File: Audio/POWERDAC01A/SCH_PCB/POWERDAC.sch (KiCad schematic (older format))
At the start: 2 parts

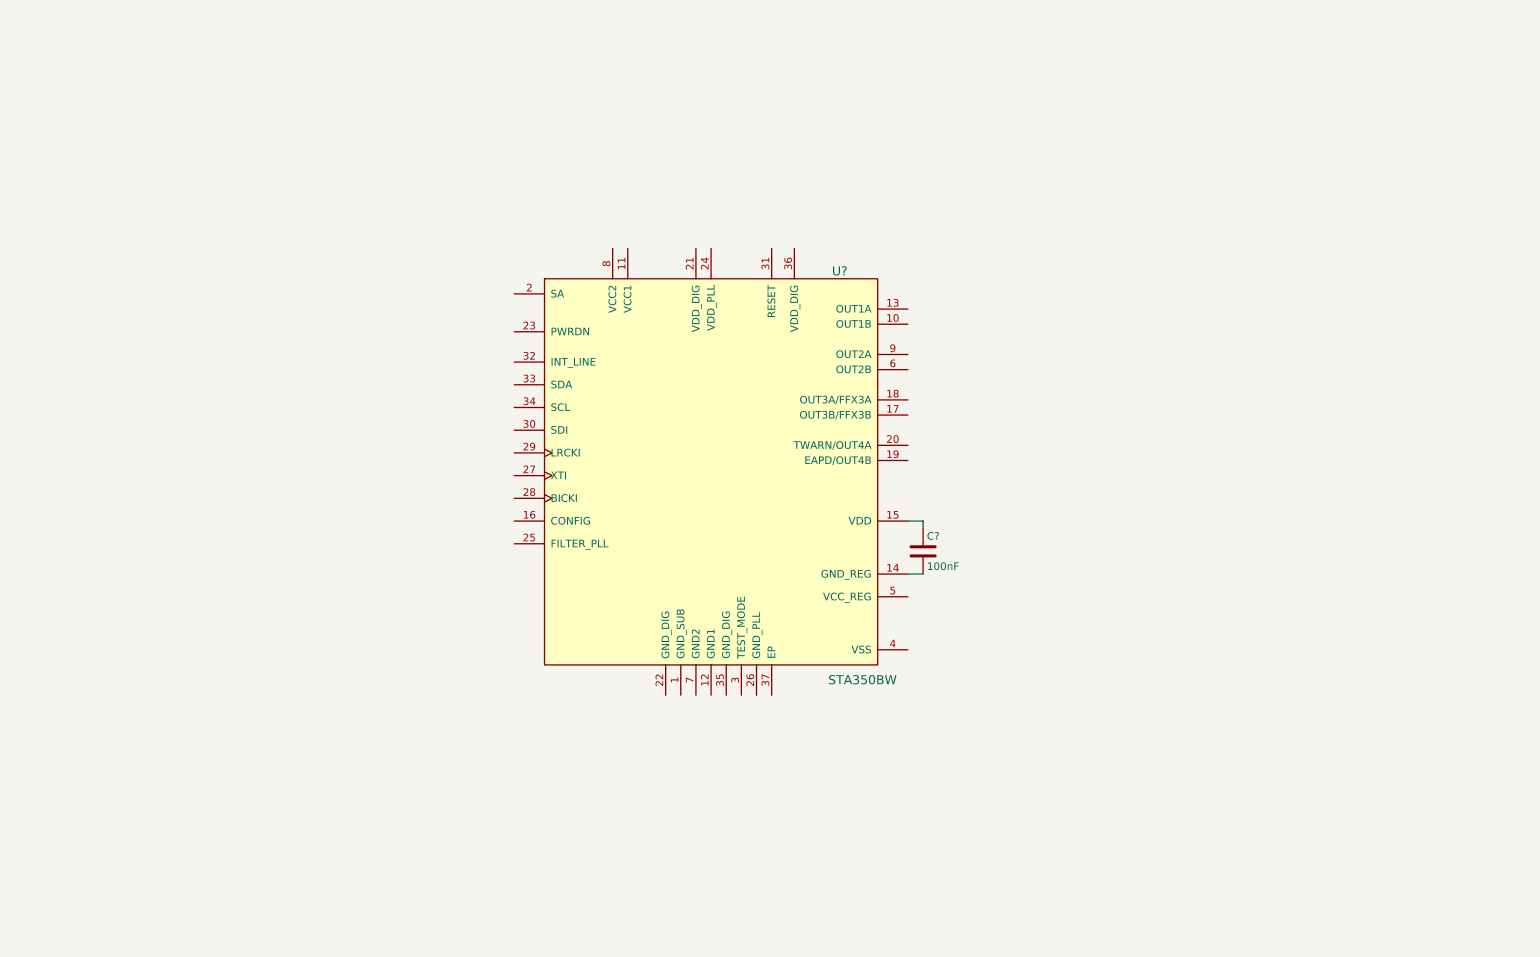
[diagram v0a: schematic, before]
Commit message: uprava prumeru hridele podle nastaveni tiskarny.
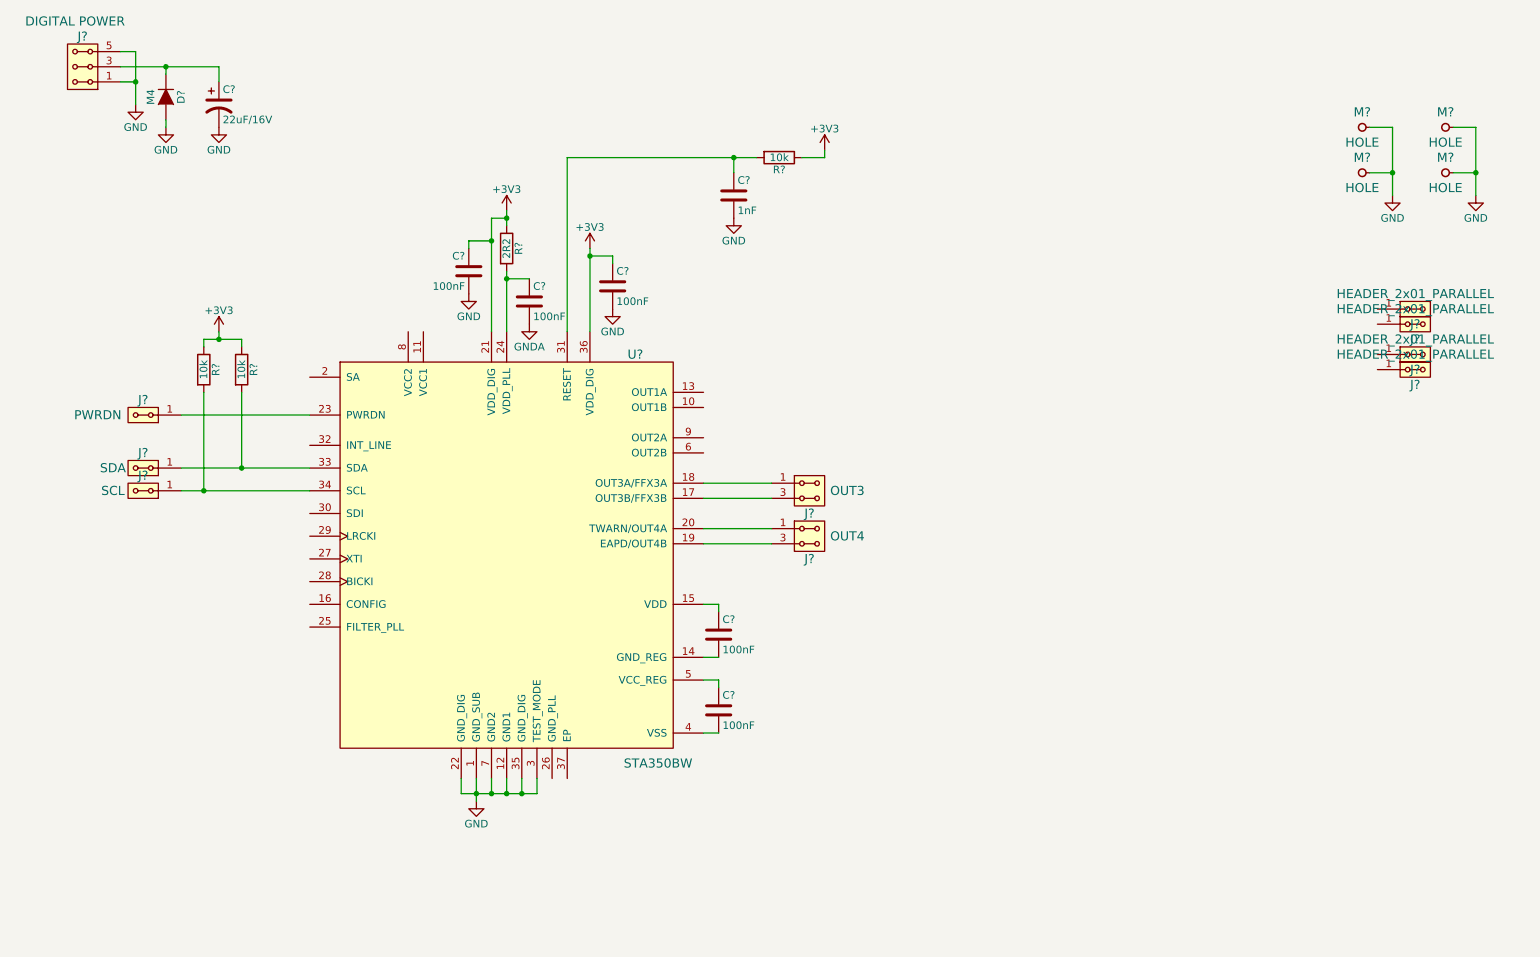
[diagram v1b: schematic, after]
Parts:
- added C? (x4): 100nF, symbol C
- added C?: 1nF, symbol C
- added C?: 22uF/16V, symbol CP1
- added D?: M4, symbol D
- added J?: PWRDN, symbol HEADER_2x01_PARALLEL
- added J?: OUT3, symbol HEADER_2x02_PARALLEL
- added J?: OUT4, symbol HEADER_2x02_PARALLEL
- added J? (x4): HEADER_2x01_PARALLEL, symbol HEADER_2x01_PARALLEL
- added J?: SDA, symbol HEADER_2x01_PARALLEL
- added J?: SCL, symbol HEADER_2x01_PARALLEL
- added J?: DIGITAL POWER, symbol HEADER_2x03_PARALLEL
- added M? (x4): HOLE, symbol HOLE
- added R? (x3): 10k, symbol R
- added R?: 2R2, symbol R
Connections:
- net GND: now reaches U?.1 (GND_SUB)
- net GND: now also U?.12 (GND1), U?.22 (GND_DIG), U?.3 (TEST_MODE), U?.35 (GND_DIG), U?.7 (GND2), C?.2, C?.2, C?.2, C?.2, D?.2 (A), J?.1, J?.2, J?.5, J?.6, M?.1, M?.1, M?.1, M?.1
- net at U?.17 (OUT3B/FFX3B): now also J?.3, J?.4
- net at U?.18 (OUT3A/FFX3A): now also J?.1, J?.2
- net at U?.19 (EAPD/OUT4B): now also J?.3, J?.4
- net at U?.20 (TWARN/OUT4A): now also J?.1, J?.2
- net +3V3: now reaches U?.21 (VDD_DIG)
- net +3V3: now also U?.36 (VDD_DIG), C?.1, C?.1, R?.1, R?.1, R?.1, R?.1
- net at U?.23 (PWRDN): now also J?.1, J?.2
- net at U?.24 (VDD_PLL): now also C?.1, R?.2
- net at U?.31 (RESET): now also C?.1, R?.2
- net at U?.33 (SDA): now also J?.1, J?.2, R?.2
- net at U?.34 (SCL): now also J?.1, J?.2, R?.2
- net at U?.4 (VSS): now also C?.2
- net at U?.5 (VCC_REG): now also C?.1
- new net: J?.1, J?.2 (x4)
- new net: C?.1, D?.1 (K), J?.3, J?.4
- new net GNDA: C?.2
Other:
- moved on the sheet: C?, U?

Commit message: zacatek navrhu noveho PCB pro modul vykonoveho zesilovace.
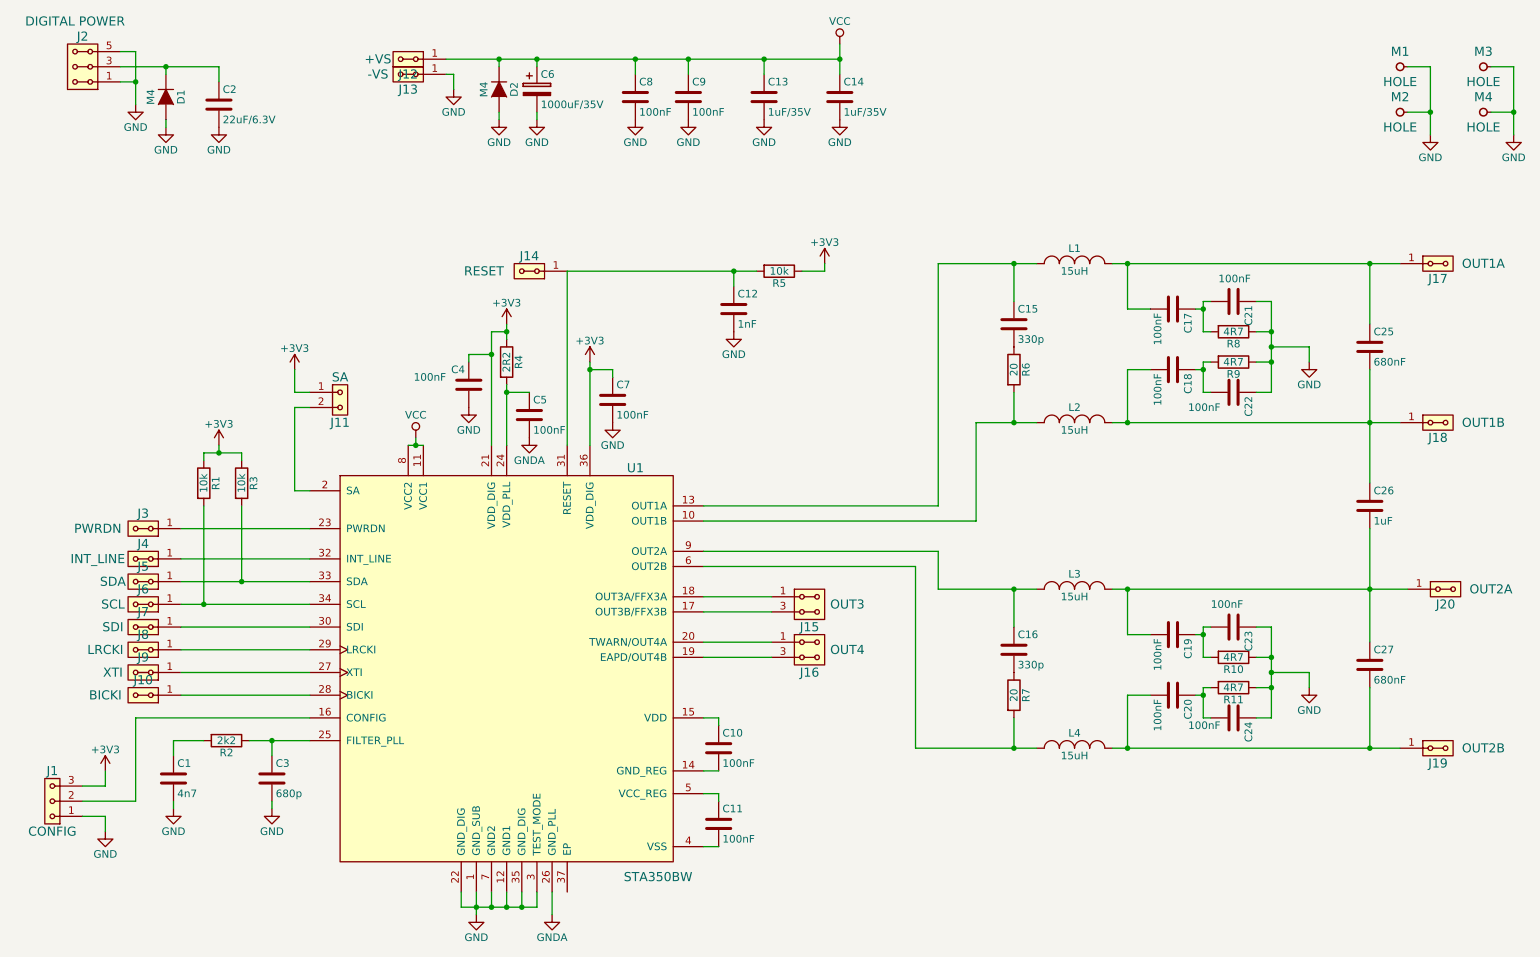
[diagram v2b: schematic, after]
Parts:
- removed C?: 22uF/16V, symbol CP1
- removed J? (x2): HEADER_2x01_PARALLEL, symbol HEADER_2x01_PARALLEL
- added C1: 4n7, Capacitors_SMD:C_0805, symbol C
- added C13, C14: 1uF/35V, Capacitors_SMD:C_1206, symbol C
- added C15, C16: 330p, Capacitors_SMD:C_0805, symbol C
- added C17, C18, C19, C20, C21, C22, C23, C24, C8, C9: 100nF, Capacitors_SMD:C_0805, symbol C
- added C2: 22uF/6.3V, Capacitors_SMD:C_0805, symbol C
- added C25, C27: 680nF, Capacitors_SMD:C_0805, symbol C
- added C26: 1uF, Capacitors_SMD:C_0805, symbol C
- added C3: 680p, Capacitors_SMD:C_0805, symbol C
- added C6: 1000uF/35V, Capacitors_ThroughHole:C_Radial_D12.5_L25_P5, symbol CP
- added D2: M4, Diodes_SMD:SMA_Standard, symbol D
- added J1: CONFIG, Mlab_Pin_Headers:Straight_1x03, symbol HEADER_1x03
- added J10: BICKI, Mlab_Pin_Headers:Straight_1x02, symbol HEADER_2x01_PARALLEL
- added J11: SA, Mlab_Pin_Headers:Straight_1x02, symbol HEADER_1x02
- added J12: +VS, Terminal_Blocks:TerminalBlock_WAGO_256_RM5mm_1pol, symbol HEADER_2x01_PARALLEL
- added J13: -VS, Terminal_Blocks:TerminalBlock_WAGO_256_RM5mm_1pol, symbol HEADER_2x01_PARALLEL
- added J14: RESET, Mlab_Pin_Headers:Straight_1x02, symbol HEADER_2x01_PARALLEL
- added J19: OUT2B, Terminal_Blocks:TerminalBlock_WAGO_256_RM5mm_1pol, symbol HEADER_2x01_PARALLEL
- added J20: OUT2A, Terminal_Blocks:TerminalBlock_WAGO_256_RM5mm_1pol, symbol HEADER_2x01_PARALLEL
- added J4: INT_LINE, Mlab_Pin_Headers:Straight_1x02, symbol HEADER_2x01_PARALLEL
- added J7: SDI, Mlab_Pin_Headers:Straight_1x02, symbol HEADER_2x01_PARALLEL
- added J8: LRCKI, Mlab_Pin_Headers:Straight_1x02, symbol HEADER_2x01_PARALLEL
- added J9: XTI, Mlab_Pin_Headers:Straight_1x02, symbol HEADER_2x01_PARALLEL
- added L1, L2, L3, L4: 15uH, Choke_SMD:Choke_SMD_12x12mm_h6mm, symbol INDUCTOR_SMALL
- added R10, R11, R8, R9: 4R7, Resistors_SMD:R_1206, symbol R
- added R2: 2k2, Resistors_SMD:R_0805, symbol R
- added R6, R7: 20, Resistors_SMD:R_1206, symbol R
- C10, C11, C12, C4, C5, C7: renamed from C?; footprint (none) -> Capacitors_SMD:C_0805
- D1: renamed from D?; footprint (none) -> Diodes_SMD:SMA_Standard
- J15, J16: renamed from J?; footprint (none) -> Mlab_Pin_Headers:Straight_2x02
- J17: renamed from J?; value HEADER_2x01_PARALLEL -> OUT1A; footprint (none) -> Terminal_Blocks:TerminalBlock_WAGO_256_RM5mm_1pol
- J18: renamed from J?; value HEADER_2x01_PARALLEL -> OUT1B; footprint (none) -> Terminal_Blocks:TerminalBlock_WAGO_256_RM5mm_1pol
- J2: renamed from J?; footprint (none) -> Mlab_Pin_Headers:Straight_2x03
- J3, J5, J6: renamed from J?; footprint (none) -> Mlab_Pin_Headers:Straight_1x02
- M1, M2, M3, M4: renamed from M?; footprint (none) -> Mlab_Mechanical:MountingHole_3mm
- R1, R3, R4, R5: renamed from R?; footprint (none) -> Resistors_SMD:R_0805
- U1: renamed from U?; footprint (none) -> Power_Packages_SMD:PowerSSO-36
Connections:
- net +3V3: now also J1.3, J11.1
- net GND: now also C1.2, C13.2, C14.2, C2.2, C21.1, C22.1, C23.1, C24.1, C3.2, C6.2, C8.2, C9.2, D2.2 (A), J1.1, J13.1, J13.2, R10.1, R11.1, R8.1, R9.1
- net GNDA: now also U1.26 (GND_PLL)
- net at U1.10 (OUT1B): now also L2.1, R6.2
- net VCC: now reaches U1.11 (VCC1)
- net VCC: now also U1.8 (VCC2), C13.1, C14.1, C6.1, C8.1, C9.1, D2.1 (K), J12.1, J12.2
- net at U1.13 (OUT1A): now also C15.1, L1.1
- net at U1.16 (CONFIG): now also J1.2
- net at U1.2 (SA): now also J11.2
- net at U1.25 (FILTER_PLL): now also C3.1, R2.1
- net at U1.27 (XTI): now also J9.1, J9.2
- net at U1.28 (BICKI): now also J10.1, J10.2
- net at U1.29 (LRCKI): now also J8.1, J8.2
- net at U1.30 (SDI): now also J7.1, J7.2
- net at C12.1, R5.2, U1.31 (RESET): now also J14.1, J14.2
- net at U1.32 (INT_LINE): now also J4.1, J4.2
- net at U1.6 (OUT2B): now also L4.1, R7.2
- net at U1.9 (OUT2A): now also C16.1, L3.1
- net at J18.1, J18.2: now also C18.2, C25.2, C26.1, L2.2
- net at J17.1, J17.2: now also C17.2, C25.1, L1.2
- net at D1.1 (K), J2.3, J2.4: now also C2.1
- new net: C1.1, R2.2
- new net: C15.2, R6.1
- new net: C17.1, C21.2, R8.2
- new net: C18.1, C22.2, R9.2
- new net: C20.2, C27.2, J19.1, J19.2, L4.2
- new net: C19.2, C26.2, C27.1, J20.1, J20.2, L3.2
- new net: C16.2, R7.1
- new net: C19.1, C23.2, R10.2
- new net: C20.1, C24.2, R11.2
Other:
- moved on the sheet: C10, C11, C12, C4, C5, C7, J15, J16, J17, J18, J3, J5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

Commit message: prace na routovani plosneho spoje.
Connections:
- net GNDA is gone; now on net GND: C5.2, U1.26 (GND_PLL)
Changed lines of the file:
@@
 	3500 6350 3500 6450
 Wire Wire Line
-	3500 6450 4000 6450
+	3500 6450 4100 6450
 Wire Wire Line
 	4000 6450 4000 6350
@@
 F 3 "" H 3800 2850 30  0000 C CNN
 	1    3800 2850
-	1    0    0    -1
-$EndComp
-$Comp
-L GNDA #PWR08
-U 1 1 55FAC3E0
-P 3950 3350
-F 0 "#PWR08" H 3950 3100 50  0001 C CNN
-F 1 "GNDA" H 3950 3200 50  0000 C CNN
-F 2 "" H 3950 3350 60  0000 C CNN
-F 3 "" H 3950 3350 60  0000 C CNN
-	1    3950 3350
 	1    0    0    -1
 $EndComp
@@
 	1    0    0    -1
 $EndComp
-$Comp
-L GNDA #PWR024
-U 1 1 55FBD329
-P 4100 6500
-F 0 "#PWR024" H 4100 6250 50  0001 C CNN
-F 1 "GNDA" H 4100 6350 50  0000 C CNN
-F 2 "" H 4100 6500 60  0000 C CNN
-F 3 "" H 4100 6500 60  0000 C CNN
-	1    4100 6500
-	1    0    0    -1
-$EndComp
-Wire Wire Line
-	4100 6500 4100 6350
 Connection ~ 6000 850
 $Comp
@@
 	1    0    0    -1
 $EndComp
+Wire Wire Line
+	4100 6450 4100 6350
+Connection ~ 4000 6450
+$Comp
+L GND #PWR?
+U 1 1 56007D42
+P 3950 3350
+F 0 "#PWR?" H 3950 3100 50  0001 C CNN
+F 1 "GND" H 3950 3200 50  0000 C CNN
+F 2 "" H 3950 3350 60  0000 C CNN
+F 3 "" H 3950 3350 60  0000 C CNN
+	1    3950 3350
+	1    0    0    -1
+$EndComp
